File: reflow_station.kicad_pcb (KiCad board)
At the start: 6 copper layers, 180 x 110 mm, 261 parts, among them IC1 MP100LGN-Z, IC2 AMC23C10DWVR, J1 1731734, J10 USB_A, J11 USB_C_Receptacle_USB2.0_16P, J12 Conn_ARM_JTAG_SWD_10, J13 F52Q-1A7H1-11015, J2 1707027, J3 1707027, J4 1707027, J5 1707027, J6 DG301-5.0-02P-12-00A_H_, J7 DG301-5.0-02P-12-00A_H_, J8 DG301-5.0-02P-12-00A_H_, J9 DG301-5.0-02P-12-00A_H_, M1 Fan_CPU_4pin, M2 Fan_CPU_4pin, M3 Fan_CPU_4pin, M4 Fan_CPU_4pin, Q1 BTA16-600B, Q2 BTA16-600B, Q3 BTA16-600B, Q4 BTA16-600B, Q5 KSC1815YTA, SW2 SW_SPST, SW3 SW_SPST, SW4 SW_SPST, SW5 SW_DIP_x08, SW6 SW_Push, SW7 SW_SPDT, SW8 SW_SPDT, U1 TPS82130, U10 TPS2051BDBVR, U11 RCLAMP0504F.TCT, U12 RCLAMP0504F.TCT, U13 RCLAMP0504F.TCT, U14 STM32F469VIT6, U2 RAC20-12SK, U3 TPS82130, U4 MOC3052, U5 MOC3052, U6 MOC3052, U7 MOC3052, U8 ADS1118IDGS, U9 ADS1118IDGS, Y1 25MHz, Y2 32.768kHz

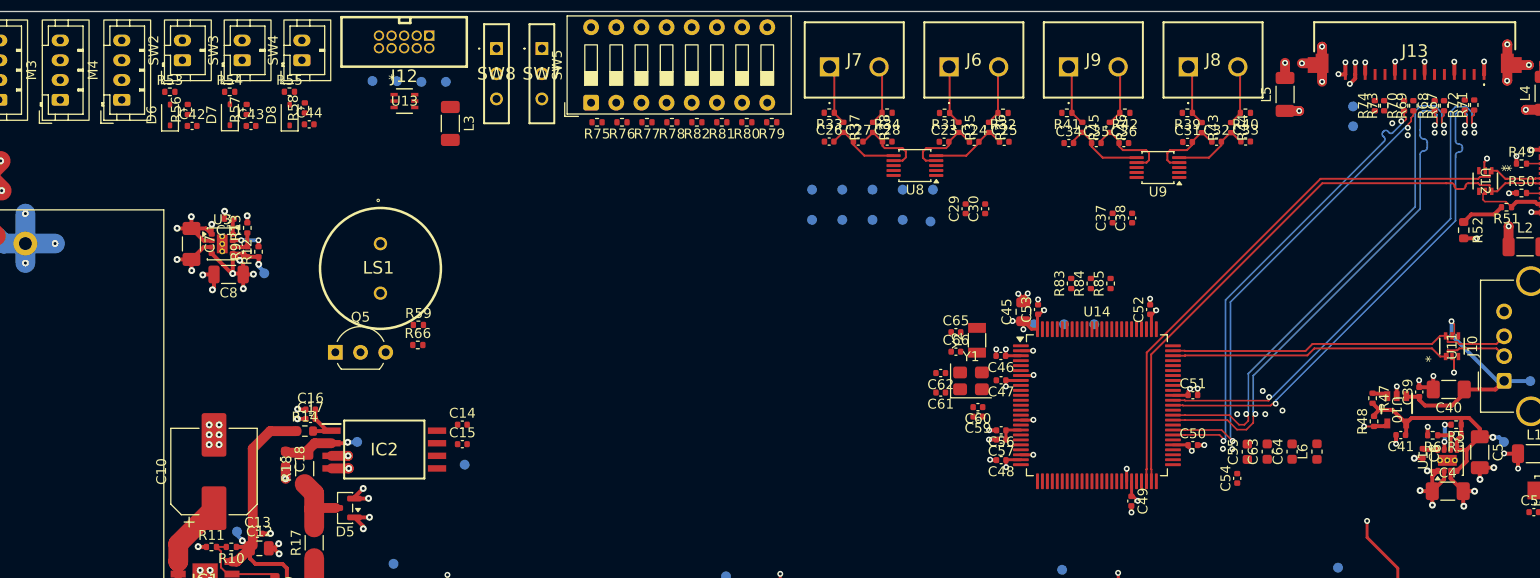
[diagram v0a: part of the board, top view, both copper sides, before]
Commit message: feat: route thermocouples, USB ports and DSI
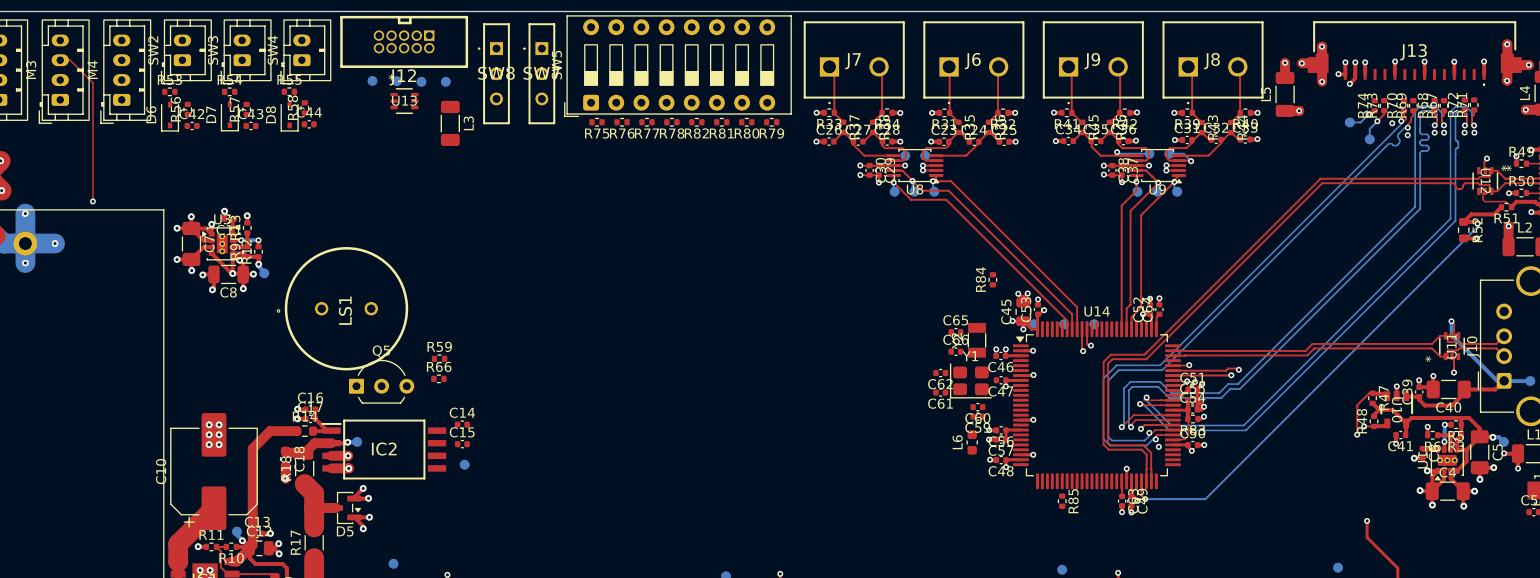
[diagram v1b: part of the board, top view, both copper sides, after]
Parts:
- C55, C63, C64: footprint reflow_station_library:C_0603_1608Metric -> reflow_station_library:C_0402_1005Metric
- moved L6 34.8 mm to (184.4, 83.5)
- moved TP19 33.8 mm to (205.1, 58.1)
- moved TP20 32.8 mm to (201.1, 58.1)
- moved TP18 28.8 mm to (203.1, 58.1)
- moved TP17 27.2 mm to (204.3, 54.3)
- moved R85 22.5 mm to (193.5, 89.4), turned to -90 degrees
- moved TP16 22.2 mm to (202.3, 54.3)
- moved C64 19.6 mm to (203.3, 70.0)
- moved R83 18.4 mm to (206.7, 81.1), turned to 180 degrees
- moved C63 15.5 mm to (199.6, 89.4), turned to -90 degrees
- moved C30 12.3 mm to (174.1, 56.0), turned to -90 degrees
- moved R84 9.90 mm to (186.5, 67.0)
- moved TP14 9.71 mm to (180.6, 58.1)
- moved C29 9.57 mm to (175.0, 56.0), turned to -90 degrees
- moved TP15 8.81 mm to (176.6, 58.1)
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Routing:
- net /Fans/FANS_IN_TACHO: track 0.00 -> 140.8 mm, vias 0 -> 1
- net /Fans/FANS_OUT_TACHO: track 0.00 -> 135.8 mm, vias 0 -> 2
- net /Connectivity/USB_UART_VBUS_SENSE: track 4.43 -> 53.1 mm, vias 0 -> 2
- net /User Interface/LCD/LCD_SCL: track 0.00 -> 41.1 mm, vias 0 -> 2
- net /User Interface/LCD/LCD_SDA: track 0.00 -> 41.1 mm, vias 0 -> 2
- net /Connectivity/USB_OC#: track 1.62 -> 40.1 mm, vias 0 -> 2
- net /Connectivity/USB_EN#: track 2.47 -> 35.4 mm, vias 1 -> 2
- net GND: track 83.2 -> 111.5 mm, vias 67 -> 86
- net /MCU/SPI_TC1_MISO: track 0.00 -> 26.7 mm, vias 0 -> 1
- net /MCU/SPI_TC1_MOSI: track 0.00 -> 25.8 mm, vias 0 -> 1
- net /MCU/SPI_TC1_CLK: track 0.00 -> 23.8 mm, vias 0 -> 1
- net /Thermocouples/SPI_TC2_MISO: track 0.00 -> 19.8 mm, vias 0 -> 1
- net /Thermocouples/SPI_TC2_CLK: track 0.00 -> 18.6 mm, vias 0 -> 1
- net /Thermocouples/SPI_TC2_MOSI: track 0.00 -> 17.2 mm, vias 0 -> 1
- net +3V3: track 52.7 -> 66.2 mm, vias 23 -> 32
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
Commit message: feat: route config switches and SWD debug
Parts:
- moved TP34 12.0 mm to (191.2, 82.1)
- moved TP35 6.89 mm to (191.5, 78.0)
- moved R84 6.72 mm to (192.6, 70.0), turned to -90 degrees
- moved C62 5.66 mm to (184.3, 81.2), turned to 0 degrees
- moved R59 4.44 mm to (135.1, 74.6)
- moved R66 4.44 mm to (135.0, 76.6)
- moved Q5 4.44 mm to (126.7, 77.4)
- moved C61 3.46 mm to (184.3, 76.8)
- moved TP36 3.23 mm to (191.5, 74.7)
- moved C65 2.82 mm to (183.3, 75.1), turned to 90 degrees
- moved L6 2.53 mm to (186.8, 84.4), turned to 0 degrees
- moved C59 2.39 mm to (187.4, 81.3)
- moved C60 2.39 mm to (187.4, 80.3)
- moved U13 2.35 mm to (127.4, 46.7)
- moved Y1 1.77 mm to (184.3, 79.0)
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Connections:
- R85 pad 1: /MCU/BOOT1 -> Net-(SW8-C)
- R85 pad 2: Net-(SW8-C) -> /MCU/BOOT1
- U13 pad 1: /Connectivity/SWDIO -> /Connectivity/SWO
- U13 pad 3: unconnected-(U13-Pad3) -> /Connectivity/RESET#
- U13 pad 4: /Connectivity/SWO -> /Connectivity/SWCLK
- U13 pad 6: /Connectivity/SWCLK -> /Connectivity/SWDIO
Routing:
- net /Device Configuration/USER_IN4#: track 0.00 -> 100.8 mm, vias 0 -> 2
- net /Connectivity/SWDIO: track 0.00 -> 99.4 mm, vias 0 -> 2
- net /Device Configuration/USER_IN3#: track 0.00 -> 95.8 mm, vias 0 -> 2
- net /Connectivity/RESET#: track 0.00 -> 93.1 mm, vias 0 -> 2
- net /Device Configuration/USER_IN2#: track 0.00 -> 91.1 mm, vias 0 -> 2
- net /Connectivity/SWCLK: track 0.00 -> 90.8 mm, vias 0 -> 2
- net /Device Configuration/USER_IN1#: track 0.00 -> 86.5 mm, vias 0 -> 2
- net /Device Configuration/TRIAC_D_ON#: track 0.00 -> 84.2 mm, vias 0 -> 2
- net /Device Configuration/TRIAC_C_ON#: track 0.00 -> 80.7 mm, vias 0 -> 2
- net Net-(SW8-C): track 0.00 -> 77.6 mm
- net /Device Configuration/TRIAC_B_ON#: track 0.00 -> 77.3 mm, vias 0 -> 2
- net /Device Configuration/TRIAC_A_ON#: track 0.00 -> 73.3 mm, vias 0 -> 2
- net Net-(SW7-C): track 0.00 -> 64.7 mm
- net +3V3: track 66.2 -> 80.5 mm, vias 32 -> 42
- net +3.3VA: track 2.46 -> 16.4 mm, vias 0 -> 2
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
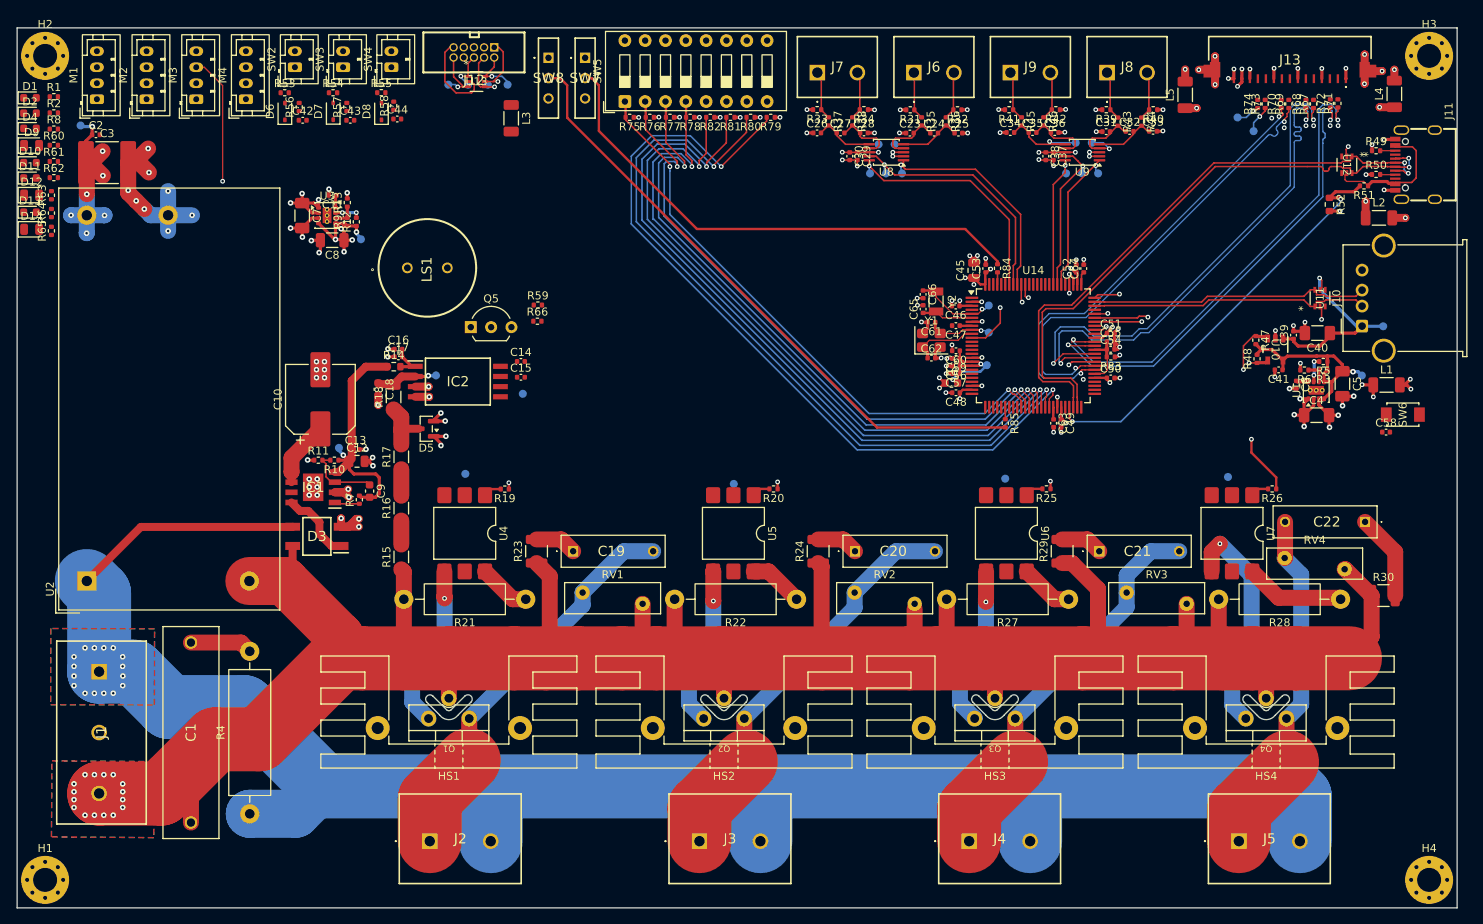
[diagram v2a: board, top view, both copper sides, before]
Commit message: feat: route remaining traces
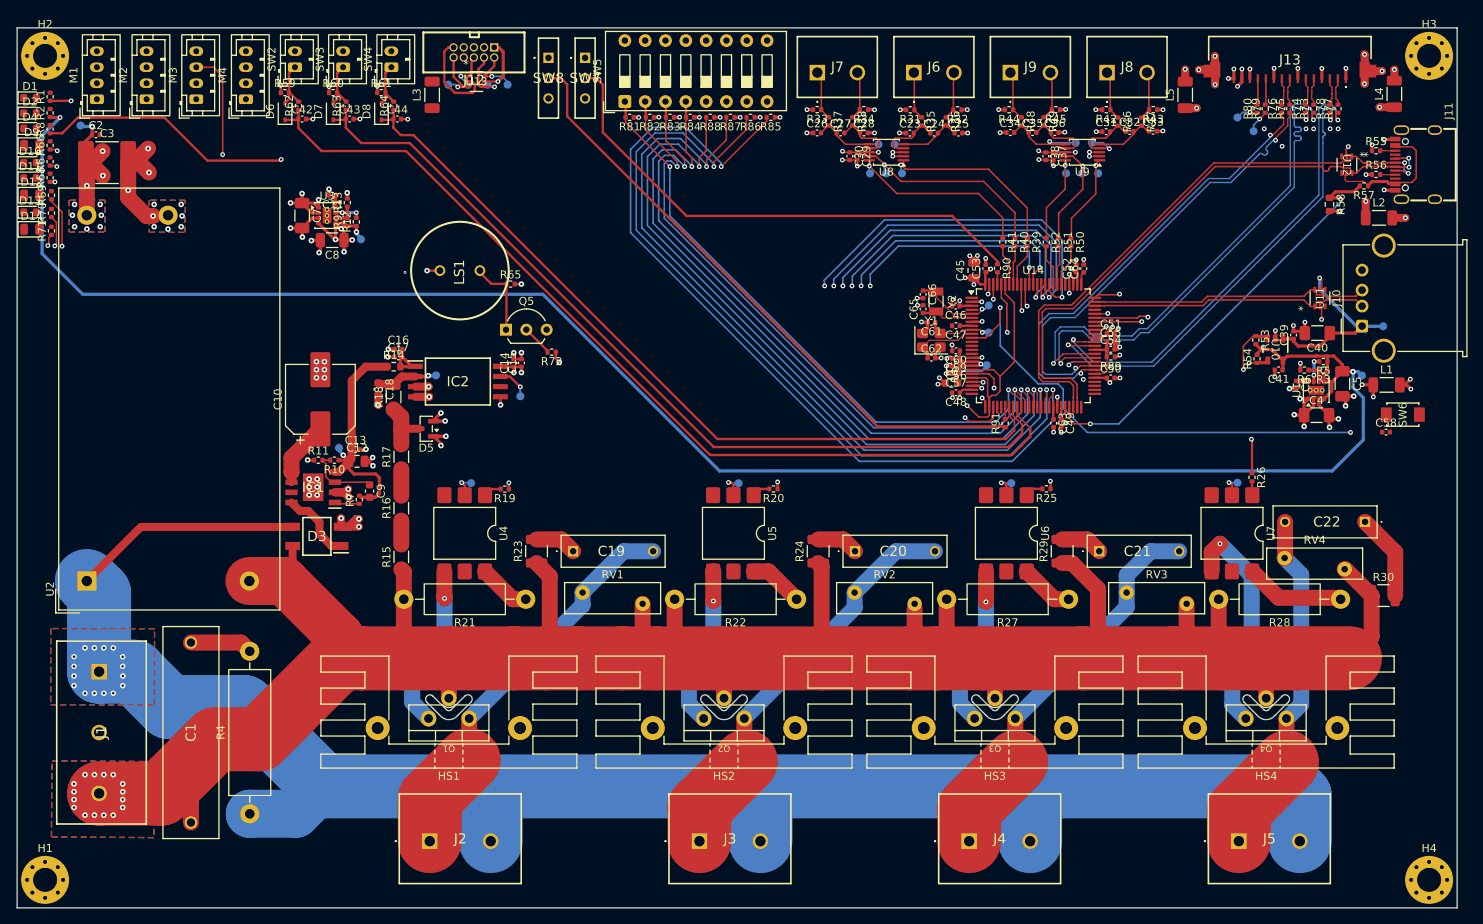
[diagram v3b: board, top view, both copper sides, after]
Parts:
- added R39: 50, reflow_station_library:R_0402_1005Metric, F.Cu at (196.3, 66.7)
- added R40: 50, reflow_station_library:R_0402_1005Metric, F.Cu at (194.8, 66.7)
- added R41: 50, reflow_station_library:R_0402_1005Metric, F.Cu at (193.2, 66.7)
- added R50: 50, reflow_station_library:R_0402_1005Metric, F.Cu at (201.7, 66.7)
- added R51: 50, reflow_station_library:R_0402_1005Metric, F.Cu at (200.2, 66.7)
- added R52: 50, reflow_station_library:R_0402_1005Metric, F.Cu at (198.7, 66.7)
- moved L3 10.3 mm to (121.9, 48.3), turned to 90 degrees
- moved R60 6.05 mm to (109.5, 48.1)
- moved D7 6.05 mm to (109.5, 50.4)
- moved SW3 6.04 mm to (110.8, 44.9)
- moved R62 6.02 mm to (105.2, 49.7)
- moved C42 6.02 mm to (105.6, 51.4)
- moved D6 6.02 mm to (103.5, 50.4)
- moved R59 6.02 mm to (103.5, 48.1)
- moved SW2 6.02 mm to (104.7, 44.9)
- moved C43 5.87 mm to (111.6, 51.4)
- moved R63 5.87 mm to (111.1, 49.7)
- moved Q5 4.42 mm to (131.1, 77.7)
- moved R65 4.30 mm to (131.7, 72.0)
- moved R72 4.26 mm to (136.8, 80.5), turned to 180 degrees
- moved LS1 4.08 mm to (125.4, 70.3)
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- renumbered C43 to C42, C42 to C43, D7 to D6, D6 to D7, R39 to R42, R40 to R43, R41 to R44, R42 to R45, R43 to R46, R44 to R47, R45 to R48, R46 to R49, R47 to R53, R48 to R54, R49 to R55, R50 to R56, R51 to R57, R52 to R58, R54 to R59, R53 to R60, R55 to R61, R57 to R62, R56 to R63, R58 to R64, R59 to R65, R60 to R66, R61 to R67, R62 to R68, R63 to R69, R64 to R70, R65 to R71, R66 to R72, R67 to R73, R68 to R74, R69 to R75, R70 to R76, R71 to R77, R72 to R78, R73 to R79, R74 to R80, R75 to R81, R76 to R82, R77 to R83, R78 to R84, R79 to R85, R80 to R86, R81 to R87, R82 to R88, R83 to R89, R84 to R90, R85 to R91, SW3 to SW2, SW2 to SW3, TP31 to TP26, TP33 to TP27, TP34 to TP28, TP35 to TP29, TP36 to TP30
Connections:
- net /User Interface/LCD/DSI1_DN0 renamed /MCU/DSI1_DN0
- net /User Interface/LCD/DSI1_DN1 renamed /MCU/DSI1_DN1
- net /User Interface/LCD/DSI1_DP0 renamed /MCU/DSI1_DP0
- net /User Interface/LCD/DSI1_DP1 renamed /MCU/DSI1_DP1
- net Net-(J13-Pad2) renamed /User Interface/LCD/CONN_DSI1_DN1
- net Net-(J13-Pad3) renamed /User Interface/LCD/CONN_DSI1_DP1
- net Net-(J13-Pad5) renamed /User Interface/LCD/CONN_DSI1_CN
- net Net-(J13-Pad6) renamed /User Interface/LCD/CONN_DSI1_CP
- net Net-(J13-Pad8) renamed /User Interface/LCD/CONN_DSI1_DN0
- net Net-(J13-Pad9) renamed /User Interface/LCD/CONN_DSI1_DP0
- TP13 pad 1: /MCU/SPI_TC1_MISO -> Net-(U8-DOUT/~{DRDY})
- TP14 pad 1: /MCU/SPI_TC1_CLK -> Net-(U8-SCLK)
- TP15 pad 1: /MCU/SPI_TC1_MOSI -> Net-(U8-DIN)
- TP18 pad 1: /Thermocouples/SPI_TC2_MISO -> Net-(U9-DOUT/~{DRDY})
- TP19 pad 1: /Thermocouples/SPI_TC2_CLK -> Net-(U9-SCLK)
- TP20 pad 1: /Thermocouples/SPI_TC2_MOSI -> Net-(U9-DIN)
- U14 pad 81: /Thermocouples/SPI_TC2_CLK -> /MCU/SPI_TC2_CLK
- U14 pad 82: /Thermocouples/SPI_TC2_MISO -> /MCU/SPI_TC2_MISO
- U14 pad 83: /Thermocouples/SPI_TC2_MOSI -> /MCU/SPI_TC2_MOSI
- U8 pad 1: /MCU/SPI_TC1_CLK -> Net-(U8-SCLK)
- U8 pad 10: /MCU/SPI_TC1_MOSI -> Net-(U8-DIN)
- U8 pad 9: /MCU/SPI_TC1_MISO -> Net-(U8-DOUT/~{DRDY})
- U9 pad 1: /Thermocouples/SPI_TC2_CLK -> Net-(U9-SCLK)
- U9 pad 10: /Thermocouples/SPI_TC2_MOSI -> Net-(U9-DIN)
- U9 pad 9: /Thermocouples/SPI_TC2_MISO -> Net-(U9-DOUT/~{DRDY})
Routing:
- net +5V: track 26.6 -> 232.9 mm, vias 1 -> 2
- net /MCU/DIODE_RUN#: track 0.00 -> 154.5 mm, vias 0 -> 3
- net /MCU/DIODE_STOP#: track 0.00 -> 152.2 mm, vias 0 -> 3
- net /MCU/DIODE_HEAT#: track 0.00 -> 150.1 mm, vias 0 -> 3
- net /MCU/DIODE_COOL#: track 0.00 -> 147.1 mm, vias 0 -> 3
- net /MCU/DIODE_FAIL#: track 0.00 -> 141.3 mm, vias 0 -> 3
- net /MCU/DIODE_TEST#: track 0.00 -> 138.1 mm, vias 0 -> 3
- net /Fans/FANS_IN_PWM: track 0.00 -> 124.6 mm, vias 0 -> 1
- net /MCU/STOP#: track 0.00 -> 117.7 mm
- net /Fans/FANS_OUT_PWM: track 0.00 -> 109.6 mm, vias 0 -> 1
- net /MCU/RUN#: track 0.00 -> 109.4 mm
- net /MCU/KILL#: track 0.00 -> 101.2 mm
- net /AC Synchronization/AC_SYNC: track 0.00 -> 92.6 mm, vias 0 -> 2
- net /Heaters/HEATER_A#: track 0.00 -> 79.4 mm, vias 0 -> 2
- net /Connectivity/RESET#: track 93.1 -> 151.4 mm, vias 2 -> 3
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- added copper zone on B.Cu, net +12V
- added copper zone on F.Cu, net +12V
- added copper zone on B.Cu, net GND
- added copper zone on F.Cu, net GND

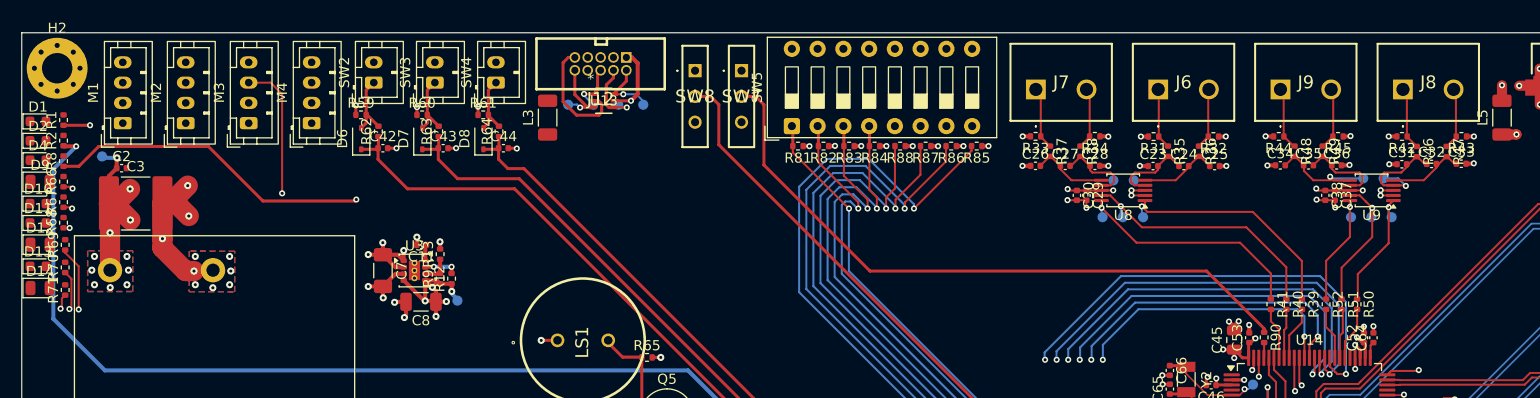
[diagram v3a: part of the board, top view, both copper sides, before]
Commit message: feat: follow pcb guidelines for thermocouples by changing capacitor and resistor positions; separate reference planes for TCs
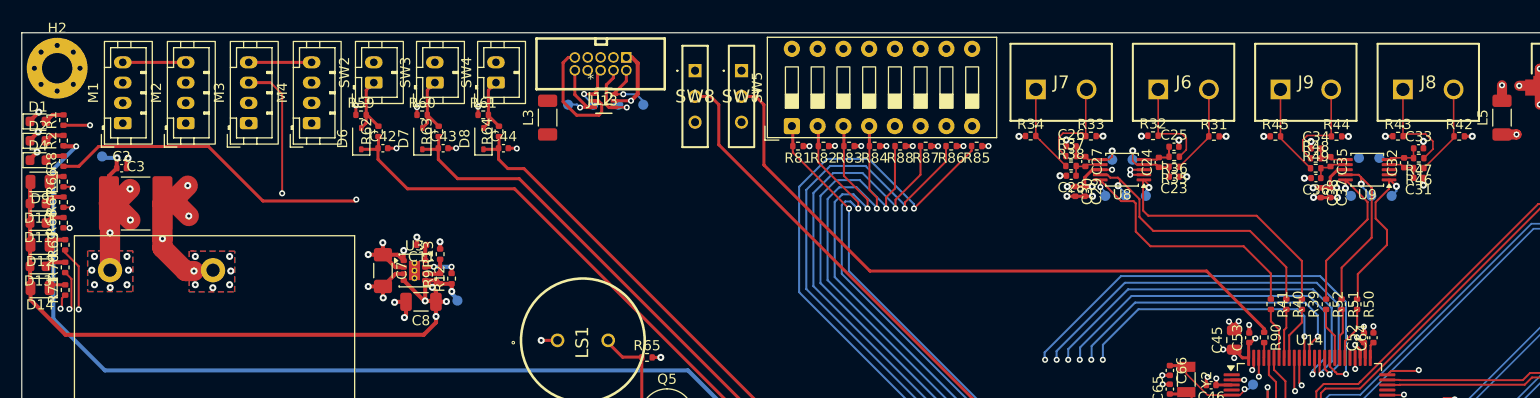
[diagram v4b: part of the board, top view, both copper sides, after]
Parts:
- moved R34 6.33 mm to (169.5, 50.1), turned to 0 degrees
- moved R43 6.26 mm to (205.8, 50.2), turned to 0 degrees
- moved R45 6.18 mm to (193.7, 50.2), turned to 0 degrees
- moved R32 5.96 mm to (181.6, 50.1), turned to 0 degrees
- moved R31 5.96 mm to (187.6, 50.2), turned to 0 degrees
- moved R44 5.70 mm to (199.7, 50.2), turned to 0 degrees
- moved R42 5.64 mm to (211.8, 50.2), turned to 0 degrees
- moved R33 5.46 mm to (175.5, 50.2), turned to 0 degrees
- moved C33 4.48 mm to (207.8, 51.4)
- moved C25 4.44 mm to (183.7, 51.2)
- moved C26 4.02 mm to (173.5, 51.2)
- moved C34 3.88 mm to (197.7, 51.4)
- moved R47 2.83 mm to (207.8, 52.3), turned to 180 degrees
- moved C32 2.71 mm to (206.4, 52.8), turned to 90 degrees
- moved C28 2.53 mm to (173.5, 54.1), turned to 180 degrees
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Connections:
- J6 pad 1: /Thermocouples/TC1+ -> /Thermocouples/TC1-
- J6 pad 2: /Thermocouples/TC1- -> /Thermocouples/TC1+
- J7 pad 1: /Thermocouples/TC3+ -> /Thermocouples/TC3-
- J7 pad 2: /Thermocouples/TC3- -> /Thermocouples/TC3+
- J8 pad 1: /Thermocouples/TC2+ -> /Thermocouples/TC2-
- J8 pad 2: /Thermocouples/TC2- -> /Thermocouples/TC2+
- J9 pad 1: /Thermocouples/TC4+ -> /Thermocouples/TC4-
- J9 pad 2: /Thermocouples/TC4- -> /Thermocouples/TC4+
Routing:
- net +3V3: track 118.1 -> 174.3 mm, vias 50 -> 51
- net Net-(U9-AIN2): track 13.4 -> 3.71 mm, vias 1 -> 0
- net Net-(U9-AIN0): track 11.5 -> 3.54 mm, vias 1 -> 0
- net /Fans/FANS_OUT_PWM: track 109.6 -> 116.6 mm
- net /Fans/FANS_IN_PWM: track 124.6 -> 130.8 mm
- net Net-(U9-AIN3): track 8.29 -> 3.55 mm
- net Net-(U9-DIN): track 11.8 -> 16.2 mm
- net Net-(U8-AIN3): track 7.74 -> 3.43 mm
- net Net-(U8-AIN1): track 7.82 -> 3.55 mm
- net Net-(U9-AIN1): track 7.68 -> 3.47 mm
- net Net-(U9-SCLK): track 12.3 -> 16.1 mm
- net /Thermocouples/TC1-: track 5.99 -> 9.71 mm
- net Net-(U9-DOUT/~{DRDY}): track 13.9 -> 17.6 mm
- net /Thermocouples/TC3+: track 6.17 -> 9.70 mm
- net /Thermocouples/TC2-: track 6.48 -> 9.98 mm
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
